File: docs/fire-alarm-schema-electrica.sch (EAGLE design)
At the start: 14 parts, among them U1 ARDUINOR3-BPLACE

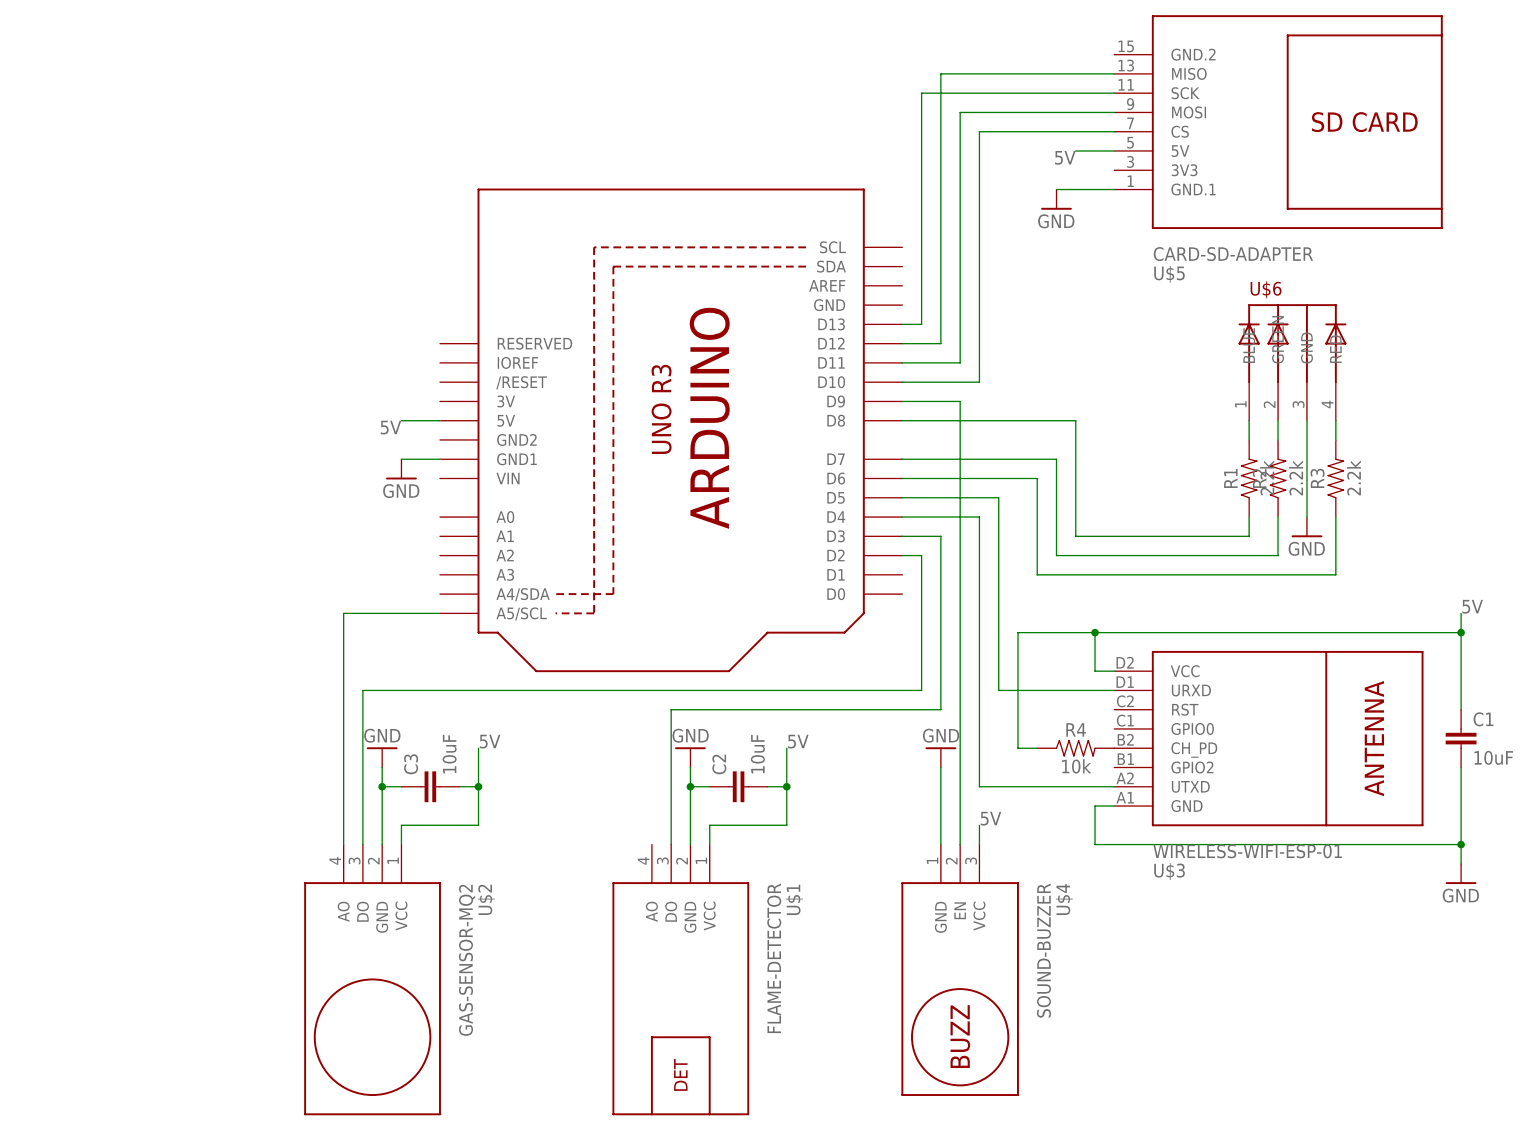
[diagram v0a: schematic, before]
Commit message: Docs: Update the IoT project documentation
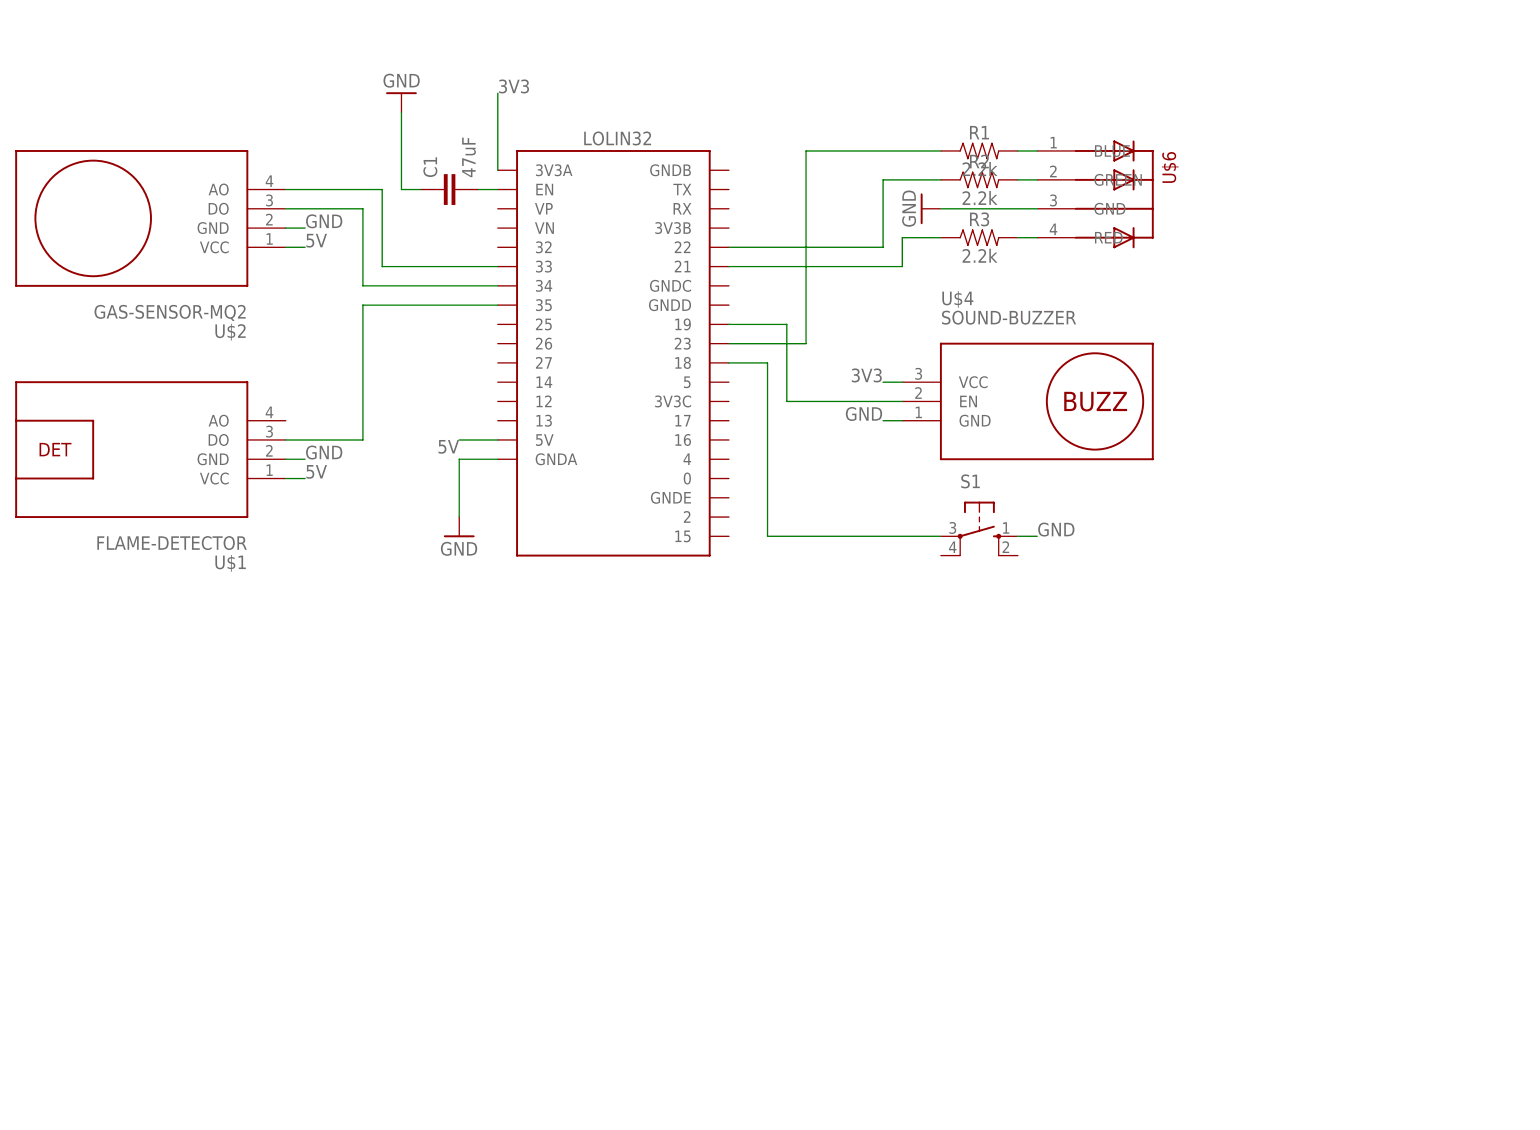
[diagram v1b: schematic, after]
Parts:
- removed C2, C3: 10uF, SparkFun-Capacitors:10UF-0603-6.3V-20%
- removed R4: 10k, SparkFun-Resistors:10KOHM-0603-1/10W-1%
- removed U$3: WIRELESS-WIFI-ESP-01, diy-modules:WIRELESS-WIFI-ESP-01
- removed U$5: CARD-SD-ADAPTER, diy-modules:CARD-SD-ADAPTER
- removed U1: ARDUINOR3-BPLACE, adafruit:ARDUINOR3-BPLACE
- added LOLIN32: (no value), SSFD - ESP32 WEMOS LOLIN CHINA W_BATT:SSFD_LOLIN32_WEMOS_CHINA_W_BATT
- added S1: (no value), switch-omron:10-XX
- C1: value 10uF -> 47uF
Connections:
- removed net N$12: R4.2, U$3.CH_PD
- removed net N$14: U$5.CS, U1.D10
- removed net N$15: U$5.MOSI, U1.D11
- removed net N$16: U$5.MISO, U1.D12
- removed net N$17: U$5.SCK, U1.D13
- new net 3V3: LOLIN32.3V3A, U$4.VCC
- net 5V: now also LOLIN32.5V; no longer C1.1, C2.2, C3.2, R4.1, U$3.VCC, U$4.VCC, U$5.5V, U1.5V
- net GND: now also C1.1, LOLIN32.GNDA, S1.S; no longer C1.2, C2.1, C3.1, U$3.GND, U$5.GND.1, U1.GND1
- net N$1: now also LOLIN32.21, R3.1; no longer U$4.EN, U1.D9
- net N$10: now also C1.2, LOLIN32.EN; no longer U$3.URXD, U1.D5
- net N$11: now also LOLIN32.35, U$1.DO; no longer U$3.UTXD, U1.D4
- net N$2: now also LOLIN32.22, R2.1; no longer U$1.DO, U1.D3
- net N$3: now also LOLIN32.33, U$2.AO; no longer U$2.DO, U1.D2
- net N$4: now also LOLIN32.34, U$2.DO; no longer U$2.AO, U1.A5/SCL
- net N$5: now also LOLIN32.23; no longer U1.D8
- net N$8: now also LOLIN32.19, U$4.EN; no longer R2.1, U1.D7
- net N$9: now also LOLIN32.18, S1.P; no longer R3.1, U1.D6
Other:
- moved on the sheet: C1, R1, R2, R3, U$1, U$2, U$4, U$6
